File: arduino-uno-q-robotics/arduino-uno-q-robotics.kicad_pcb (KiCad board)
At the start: 2 copper layers, 68.6 x 53.3 mm, 4 parts, among them J1 Conn_02x30_Odd_Even, J2 Conn_02x30_Odd_Even, J3 Connector_FFC-FPC, J4 Connector_FFC-FPC

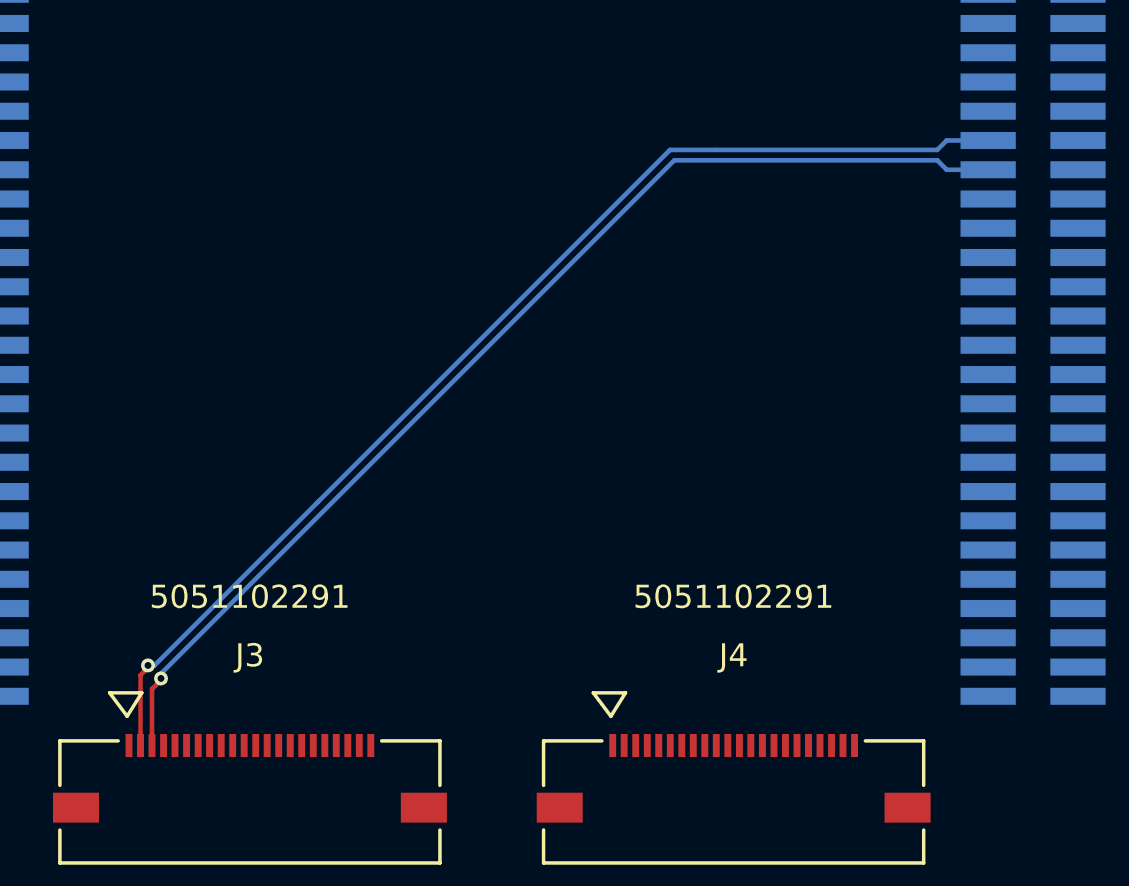
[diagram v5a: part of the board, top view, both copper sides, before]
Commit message: Update PCB constrains for 4 layer board
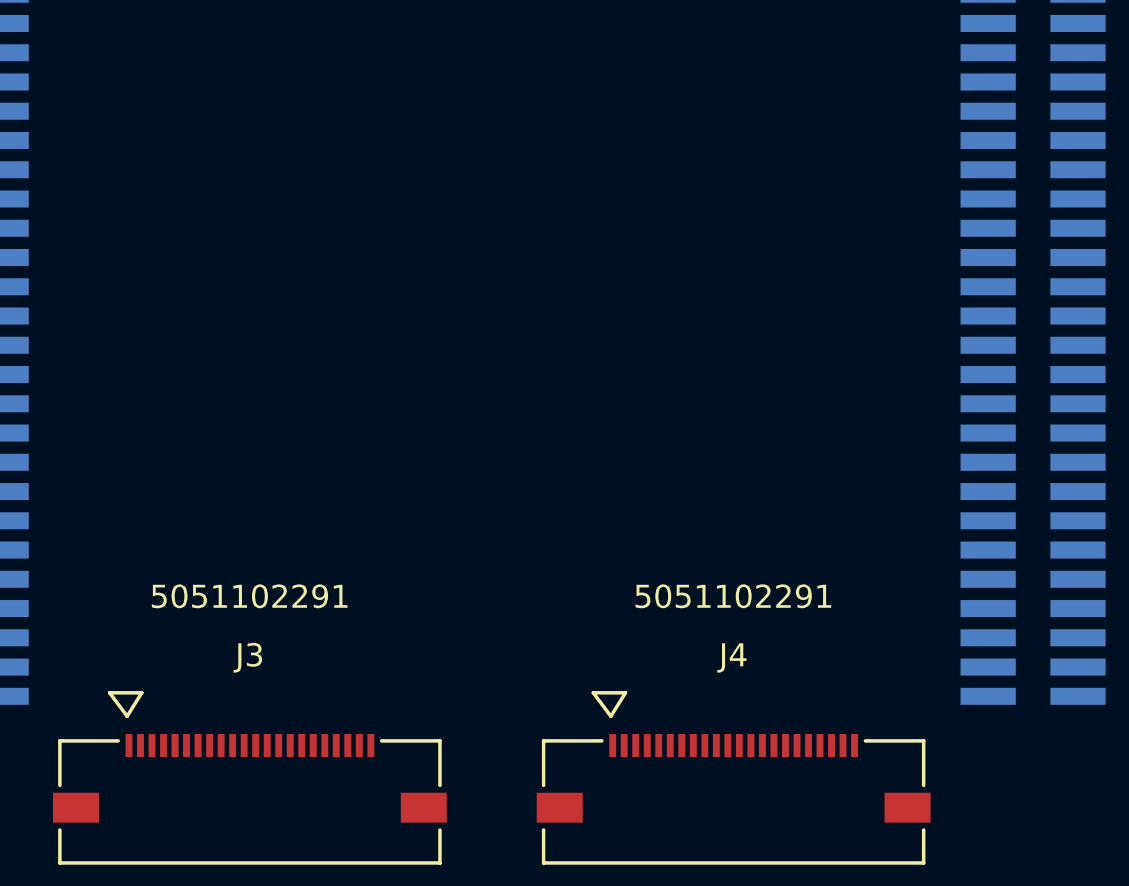
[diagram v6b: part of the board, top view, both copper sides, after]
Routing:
- net /CSI0_LN0_N: track 49.5 -> 0.00 mm, vias 1 -> 0
- net /CSI0_LN0_P: track 48.6 -> 0.00 mm, vias 1 -> 0
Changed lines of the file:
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@@
-	)
-	(segment
-		(start 134.574478 110.324478)
-		(end 134.574478 110.42552)
-		(width 0.2)
-		(layer "F.Cu")
-		(net 87)
-	)
-	(segment
-		(start 134.574478 110.42552)
-		(end 134.249999 110.749999)
-		(width 0.2)
-		(layer "F.Cu")
-		(net 87)
-	)
-	(segment
-		(start 134.249999 110.749999)
-		(end 134.249999 113.8)
-		(width 0.2)
-		(layer "F.Cu")
-		(net 87)
-	)
-	(via
-		(at 134.574478 110.324478)
-		(size 0.6)
-		(drill 0.3)
-		(layers "F.Cu" "B.Cu")
-		(net 87)
-	)
-	(segment
-		(start 157.236801 87.945)
-		(end 159.190834 87.945)
-		(width 0.2)
-		(layer "B.Cu")
-		(net 87)
-	)
-	(segment
-		(start 134.574478 110.324478)
-		(end 134.857323 110.324478)
-		(width 0.2)
-		(layer "B.Cu")
-		(net 87)
-	)
-	(segment
-		(start 134.857323 110.324478)
-		(end 141.951469 103.230332)
-		(width 0.2)
-		(layer "B.Cu")
-		(net 87)
-	)
-	(segment
-		(start 169.249999 87.535)
-		(end 171.05 87.535)
-		(width 0.2)
-		(layer "B.Cu")
-		(net 87)
-	)
-	(segment
-		(start 168.839999 87.945)
-		(end 169.249999 87.535)
-		(width 0.2)
-		(layer "B.Cu")
-		(net 87)
-	)
-	(segment
-		(start 159.190834 87.945)
-		(end 168.839999 87.945)
-		(width 0.2)
-		(layer "B.Cu")
-		(net 87)
-	)
-	(segment
-		(start 141.951469 103.230332)
-		(end 157.236801 87.945)
-		(width 0.2)
-		(layer "B.Cu")
-		(net 87)
-	)
-	(segment
-		(start 135.140165 110.890165)
-		(end 135.140165 110.960877)
-		(width 0.2)
-		(layer "F.Cu")
-		(net 88)
 	)
 	(segment
@@
 		(width 0.2)
 		(layer "F.Cu")
-		(net 88)
-	)
-	(segment
-		(start 134.75 111.351042)
-		(end 134.75 113.799999)
-		(width 0.2)
-		(layer "F.Cu")
-		(net 88)
-	)
-	(segment
-		(start 135.140165 110.960877)
-		(end 134.75 111.351042)
-		(width 0.2)
-		(layer "F.Cu")
-		(net 88)
-	)
-	(via
-		(at 135.140165 110.890165)
-		(size 0.6)
-		(drill 0.3)
-		(layers "F.Cu" "B.Cu")
-		(net 88)
-	)
-	(segment
-		(start 168.839999 88.395)
-		(end 169.249999 88.805)
-		(width 0.2)
-		(layer "B.Cu")
-		(net 88)
-	)
-	(segment
-		(start 135.140165 110.890165)
-		(end 135.140165 110.678034)
-		(width 0.2)
-		(layer "B.Cu")
-		(net 88)
-	)
-	(segment
-		(start 157.423199 88.395)
-		(end 168.839999 88.395)
-		(width 0.2)
-		(layer "B.Cu")
-		(net 88)
-	)
-	(segment
-		(start 169.249999 88.805)
-		(end 171.05 88.805)
-		(width 0.2)
-		(layer "B.Cu")
-		(net 88)
-	)
-	(segment
-		(start 135.140165 110.678034)
-		(end 157.423199 88.395)
-		(width 0.2)
-		(layer "B.Cu")
 		(net 88)
 	)
@@
 		)
 	)
-	(generated
-		(type tuning_pattern)
-		(name "Tuning Pattern")
-		(layer "B.Cu")
-		(base_line
-			(pts
-				(xy 141.951469 103.230332) (xy 157.236801 87.945) (xy 159.190834 87.945)
-			)
-		)
-		(base_line_coupled
-			(pts
-				(xy 142.269668 103.548531) (xy 142.279185 103.539014)
-			)
-		)
-		(corner_radius_percent 80)
-		(end
-			(xy 159.190834 87.945)
-		)
-		(initial_side "left")
-		(last_diff_pair_gap 0.18)
-		(last_netname "/CSI0_LN0_N")
-		(last_status "too_long")
-		(last_track_width 0.2)
-		(last_tuning "1.3462 mm (too long)")
-		(max_amplitude 1)
-		(min_amplitude 0.2)
-		(min_spacing 0.6)
-		(origin
-			(xy 141.951469 103.230332)
-		)
-		(override_custom_rules no)
-		(rounded yes)
-		(single_sided no)
-		(target_length 1000000)
-		(target_length_max 1000000)
-		(target_length_min 0)
-		(target_skew 0)
-		(target_skew_max 0.1)
-		(target_skew_min -0.1)
-		(tuning_mode "diff_pair_skew")
-		(members "09c48609-23a5-47f1-804c-d8c03bbdc80e" "ebd18ff3-89a4-4da8-9f0c-0952fc0afc23")
-	)
 	(embedded_fonts no)

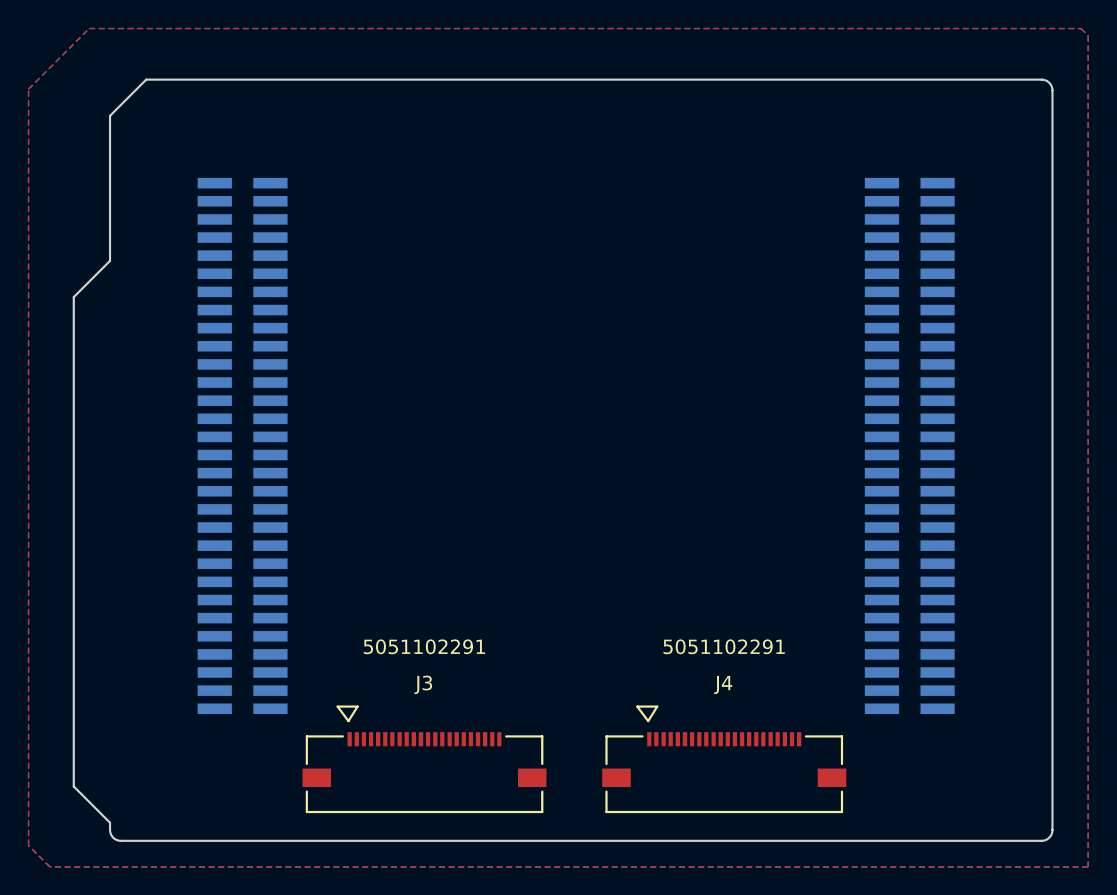
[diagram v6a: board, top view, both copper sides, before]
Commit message: Make board 4 layers
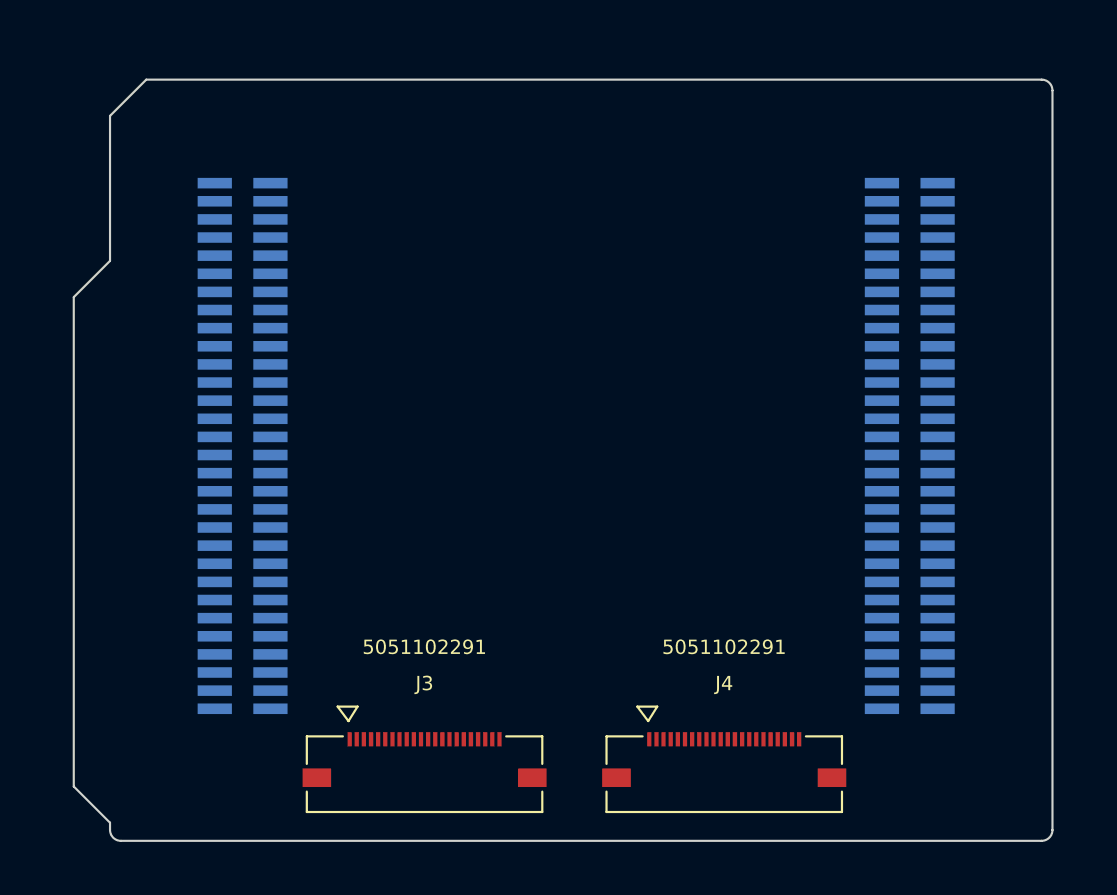
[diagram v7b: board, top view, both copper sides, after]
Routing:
- added copper zone on In1.Cu, net GND
- added copper zone on In2.Cu, net GND
- removed copper zone on B.Cu, net GND
- removed copper zone on F.Cu, net GND
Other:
- copper layers 2 -> 4
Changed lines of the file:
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@@
 	(layers
 		(0 "F.Cu" signal)
+		(4 "In1.Cu" signal)
+		(6 "In2.Cu" signal)
 		(2 "B.Cu" signal)
 		(9 "F.Adhes" user "F.Adhesive")
@@
 			)
 			(layer "dielectric 1"
+				(type "prepreg")
+				(thickness 0.1)
+				(material "FR4")
+				(epsilon_r 4.5)
+				(loss_tangent 0.02)
+			)
+			(layer "In1.Cu"
+				(type "copper")
+				(thickness 0.035)
+			)
+			(layer "dielectric 2"
 				(type "core")
-				(thickness 1.51)
+				(thickness 1.24)
+				(material "FR4")
+				(epsilon_r 4.5)
+				(loss_tangent 0.02)
+			)
+			(layer "In2.Cu"
+				(type "copper")
+				(thickness 0.035)
+			)
+			(layer "dielectric 3"
+				(type "prepreg")
+				(thickness 0.1)
 				(material "FR4")
 				(epsilon_r 4.5)
@@
 		(net 5)
 		(net_name "GND")
-		(layers "F.Cu" "B.Cu")
+		(layers "In1.Cu" "In2.Cu")
 		(hatch edge 0.5)
 		(connect_pads

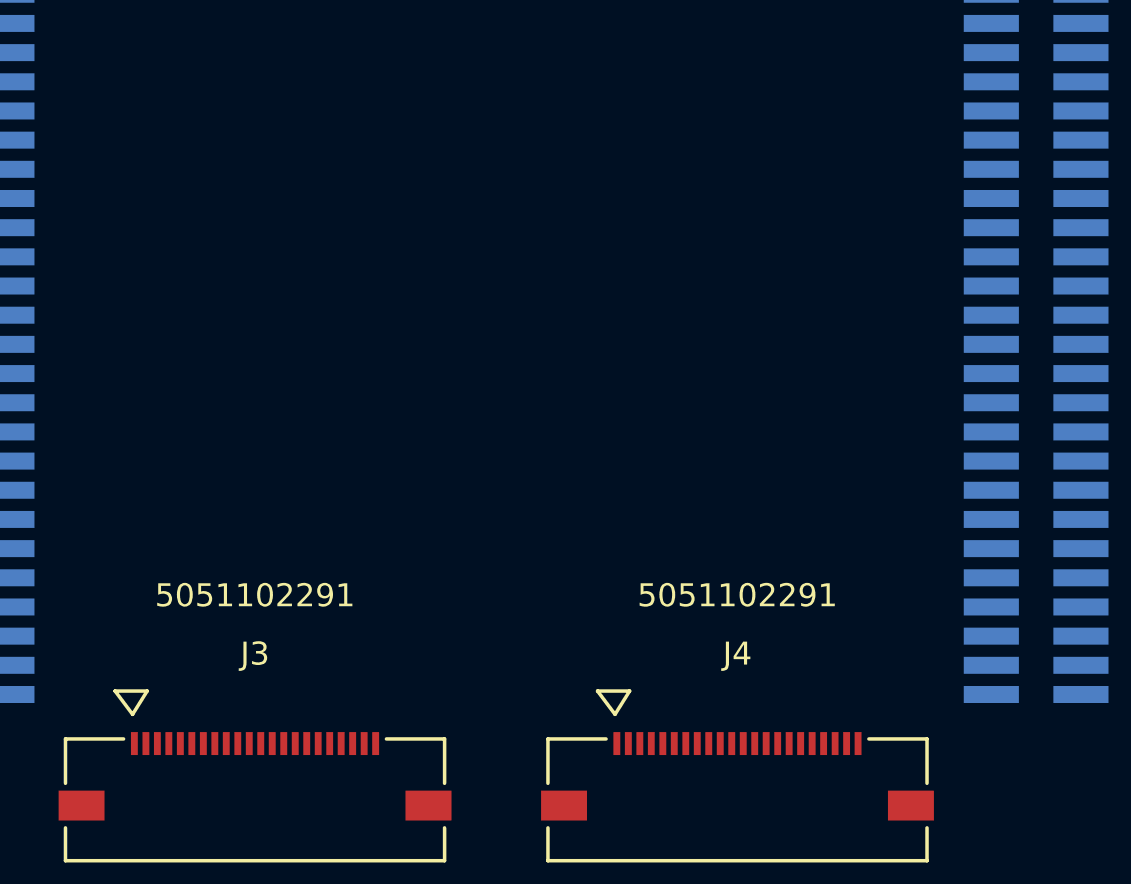
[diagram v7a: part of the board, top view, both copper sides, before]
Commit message: Connect J3 camera header signals
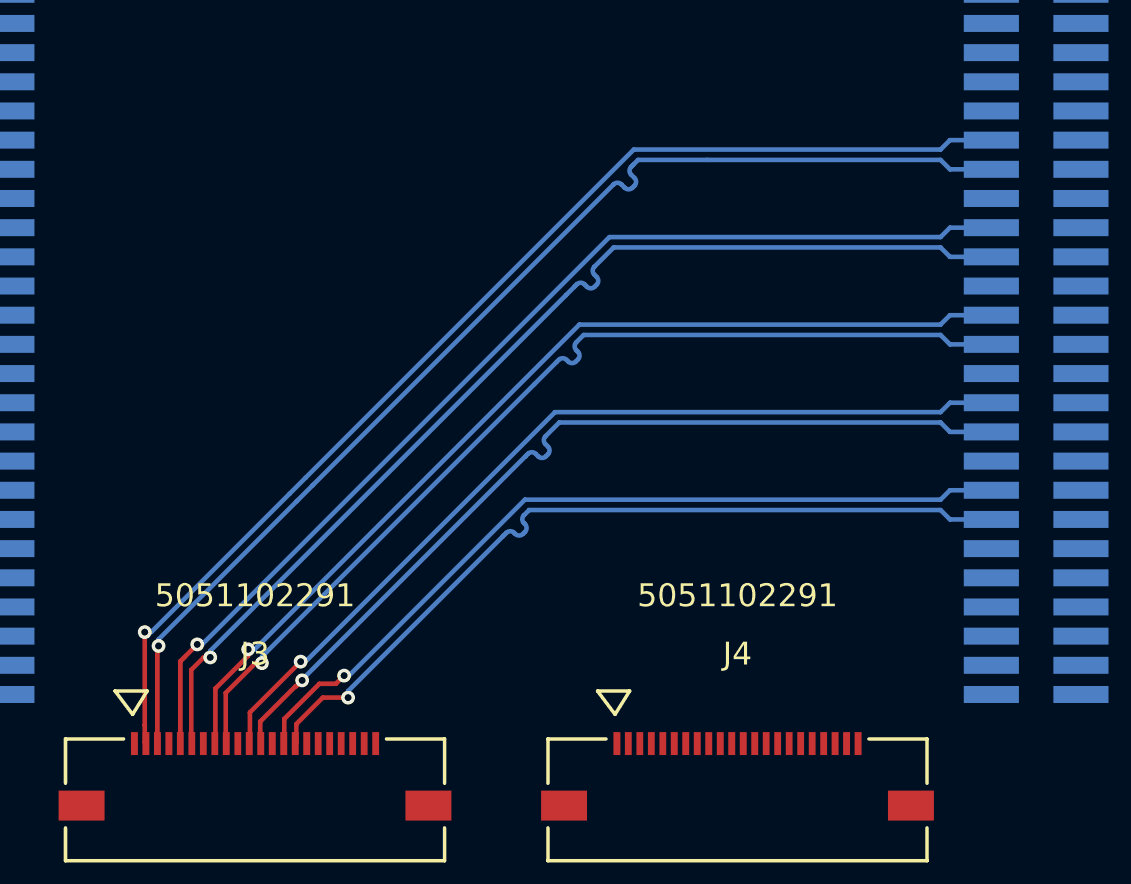
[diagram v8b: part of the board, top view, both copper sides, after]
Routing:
- net /CSI0_LN0_P: track 0.00 -> 50.6 mm, vias 0 -> 1
- net /CSI0_LN0_N: track 0.00 -> 50.6 mm, vias 0 -> 1
- net /CSI0_LN1_N: track 0.00 -> 46.8 mm, vias 0 -> 1
- net /CSI0_LN1_P: track 0.00 -> 46.8 mm, vias 0 -> 1
- net /CSI0_CLK_N: track 0.00 -> 43.1 mm, vias 0 -> 1
- net /CSI0_CLK_P: track 0.00 -> 43.0 mm, vias 0 -> 1
- net /CSI0_LN2_N: track 0.00 -> 39.2 mm, vias 0 -> 1
- net /CSI0_LN2_P: track 0.00 -> 39.2 mm, vias 0 -> 1
- net /CSI0_LN3_N: track 0.00 -> 36.0 mm, vias 0 -> 1
- net /CSI0_LN3_P: track 0.00 -> 36.0 mm, vias 0 -> 1
